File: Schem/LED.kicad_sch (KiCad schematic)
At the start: 25 parts

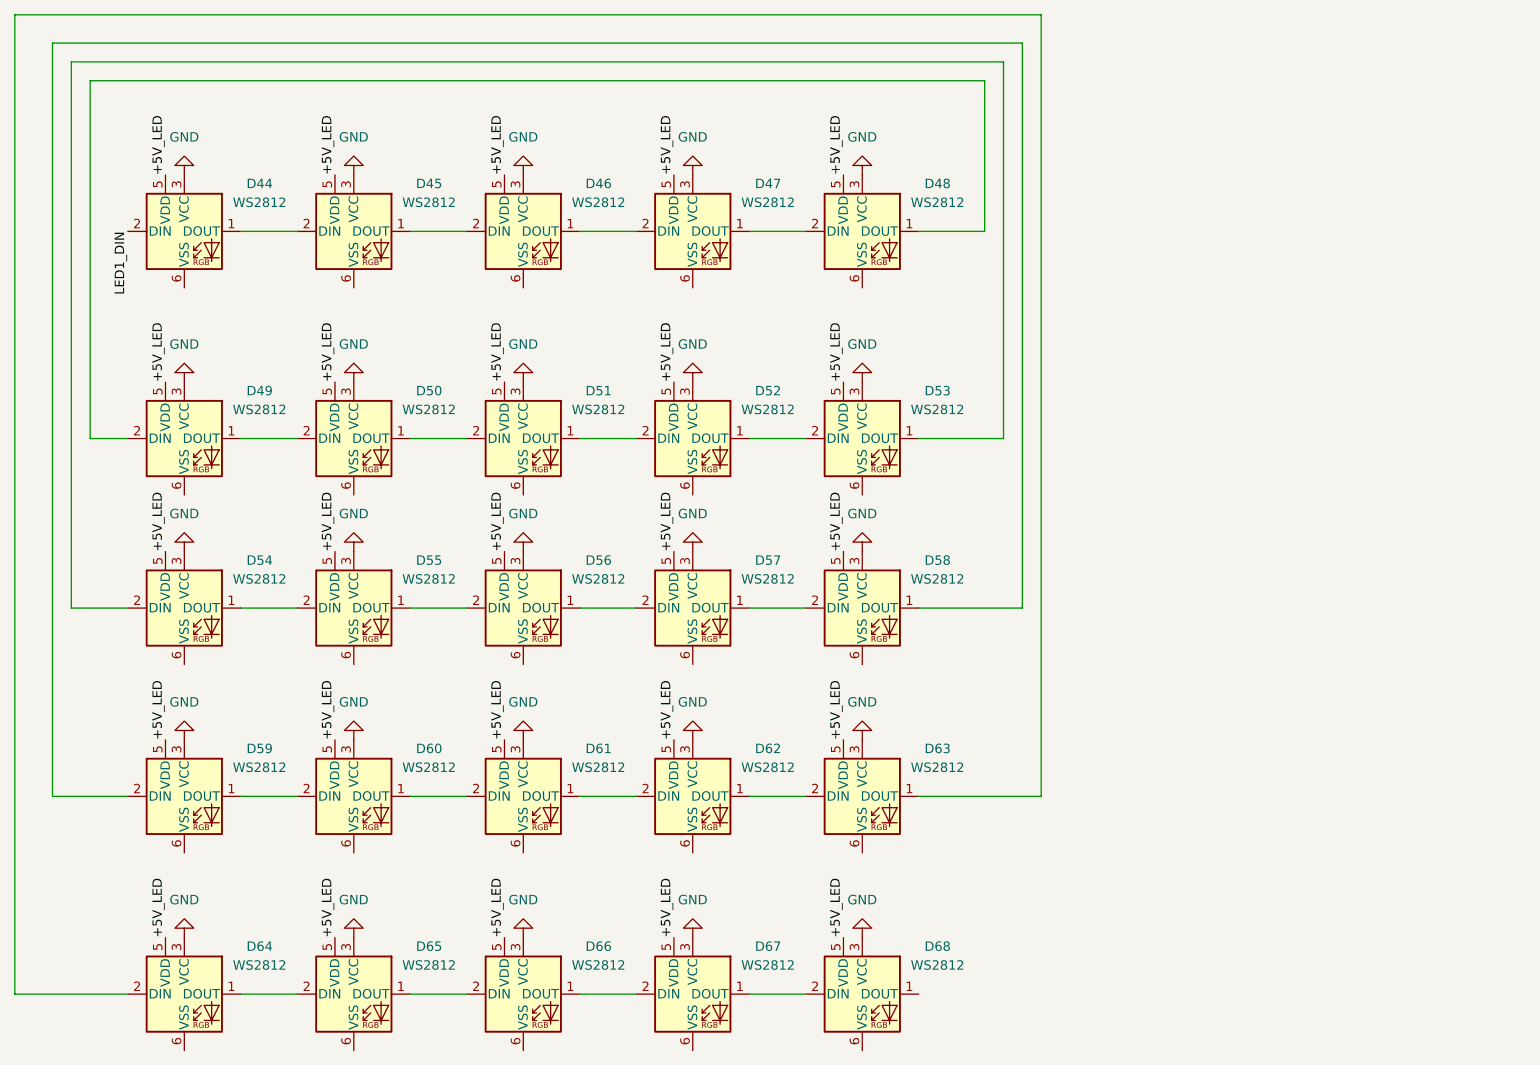
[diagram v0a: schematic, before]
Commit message: Update Schematic fixing errors (consult journal)
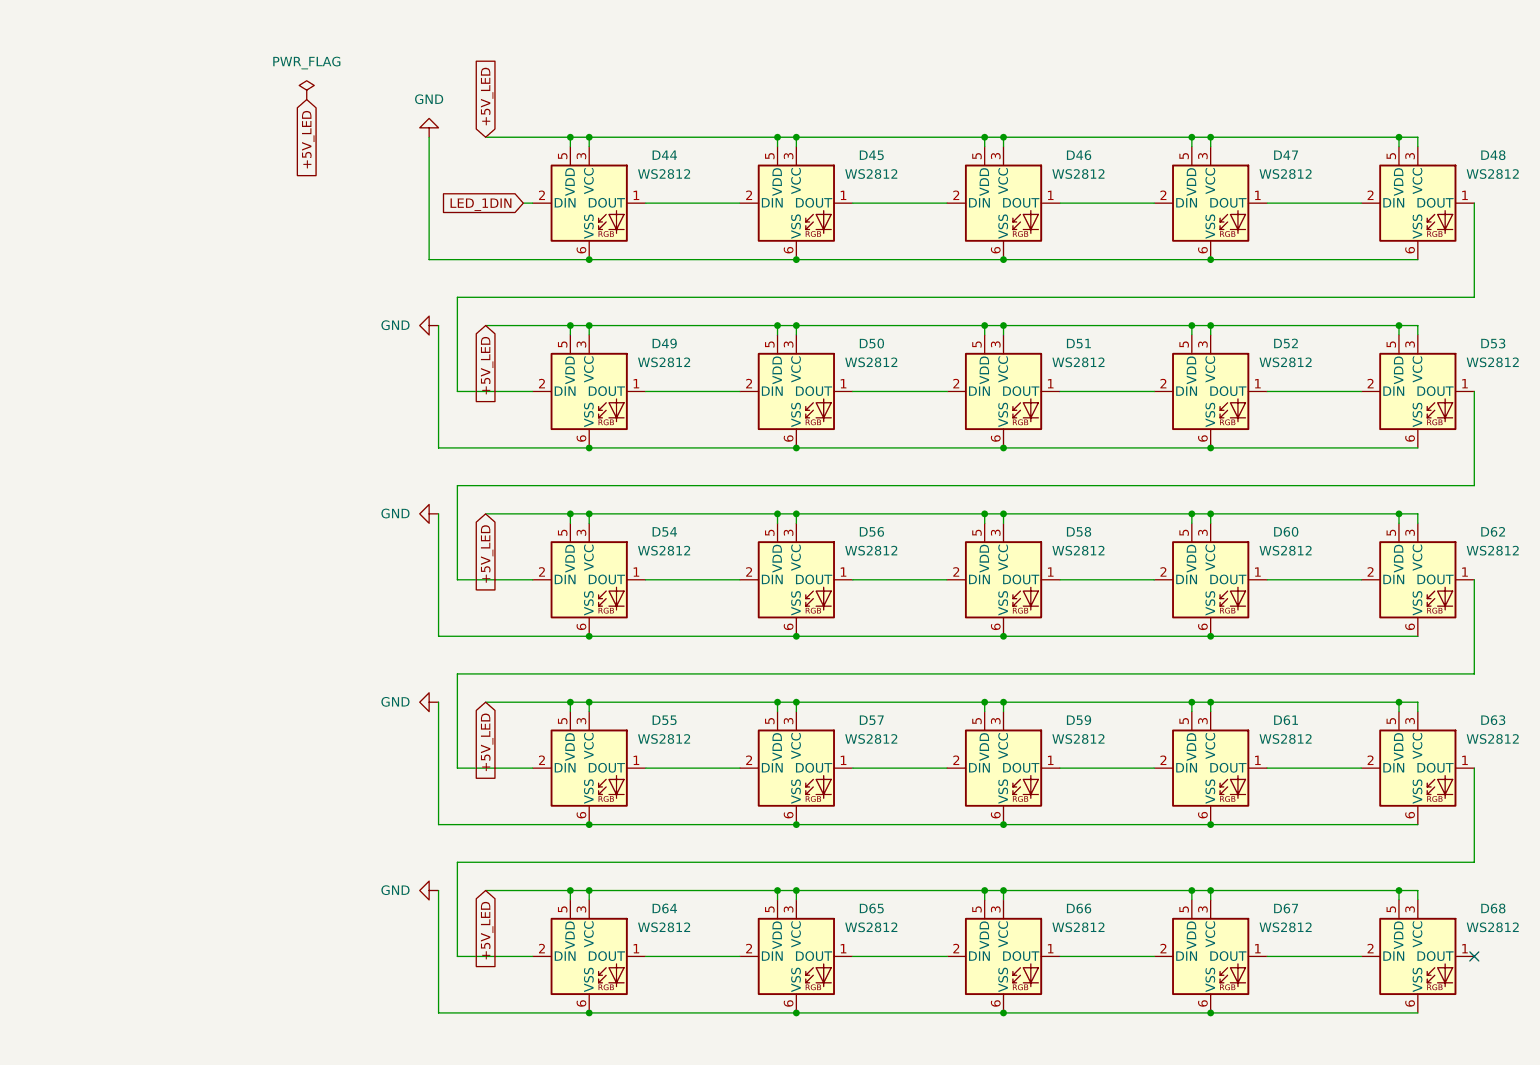
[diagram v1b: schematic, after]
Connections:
- net +5V_LED: now also D44.3 (VCC), D45.3 (VCC), D46.3 (VCC), D47.3 (VCC), D48.3 (VCC), D49.3 (VCC), D50.3 (VCC), D51.3 (VCC), D52.3 (VCC), D53.3 (VCC), D54.3 (VCC), D55.3 (VCC), D56.3 (VCC), D57.3 (VCC), D58.3 (VCC), D59.3 (VCC), D60.3 (VCC), D61.3 (VCC), D62.3 (VCC), D63.3 (VCC), D64.3 (VCC), D65.3 (VCC), D66.3 (VCC), D67.3 (VCC), D68.3 (VCC)
- net GND: now also D44.6 (VSS), D45.6 (VSS), D46.6 (VSS), D47.6 (VSS), D48.6 (VSS), D49.6 (VSS), D50.6 (VSS), D51.6 (VSS), D52.6 (VSS), D53.6 (VSS), D54.6 (VSS), D55.6 (VSS), D56.6 (VSS), D57.6 (VSS), D58.6 (VSS), D59.6 (VSS), D60.6 (VSS), D61.6 (VSS), D62.6 (VSS), D63.6 (VSS), D64.6 (VSS), D65.6 (VSS), D66.6 (VSS), D67.6 (VSS), D68.6 (VSS); no longer D44.3 (VCC), D45.3 (VCC), D46.3 (VCC), D47.3 (VCC), D48.3 (VCC), D49.3 (VCC), D50.3 (VCC), D51.3 (VCC), D52.3 (VCC), D53.3 (VCC), D54.3 (VCC), D55.3 (VCC), D56.3 (VCC), D57.3 (VCC), D58.3 (VCC), D59.3 (VCC), D60.3 (VCC), D61.3 (VCC), D62.3 (VCC), D63.3 (VCC), D64.3 (VCC), D65.3 (VCC), D66.3 (VCC), D67.3 (VCC), D68.3 (VCC)
- net at D63.2 (DIN): now also D61.1 (DOUT); no longer D62.1 (DOUT)
- net at D62.2 (DIN): now also D60.1 (DOUT); no longer D61.1 (DOUT)
- net at D61.2 (DIN): now also D59.1 (DOUT); no longer D60.1 (DOUT)
- net at D56.2 (DIN): now also D54.1 (DOUT); no longer D55.1 (DOUT)
- net at D55.2 (DIN): now also D62.1 (DOUT); no longer D54.1 (DOUT)
- net at D56.1 (DOUT): now also D58.2 (DIN); no longer D57.2 (DIN)
- net at D57.1 (DOUT): now also D59.2 (DIN); no longer D58.2 (DIN)
- net at D58.1 (DOUT): now also D60.2 (DIN); no longer D59.2 (DIN)
- net LED1_DIN renamed LED_1DIN
- new net: D55.1 (DOUT), D57.2 (DIN)
- no-connect marks 0 -> 1
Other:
- moved on the sheet: D44
